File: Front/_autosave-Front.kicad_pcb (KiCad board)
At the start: 2 copper layers, 40 x 40 mm, 42 parts, among them J1 USB_B_Micro, Q1 BC849, Q2 BC849, SW1 SW_DPDT_x2, U1 CH340C, U10 ESP32-WROOM-32, U2 CJVL53L0XV2, U3 SPX3819M5-L-3-3

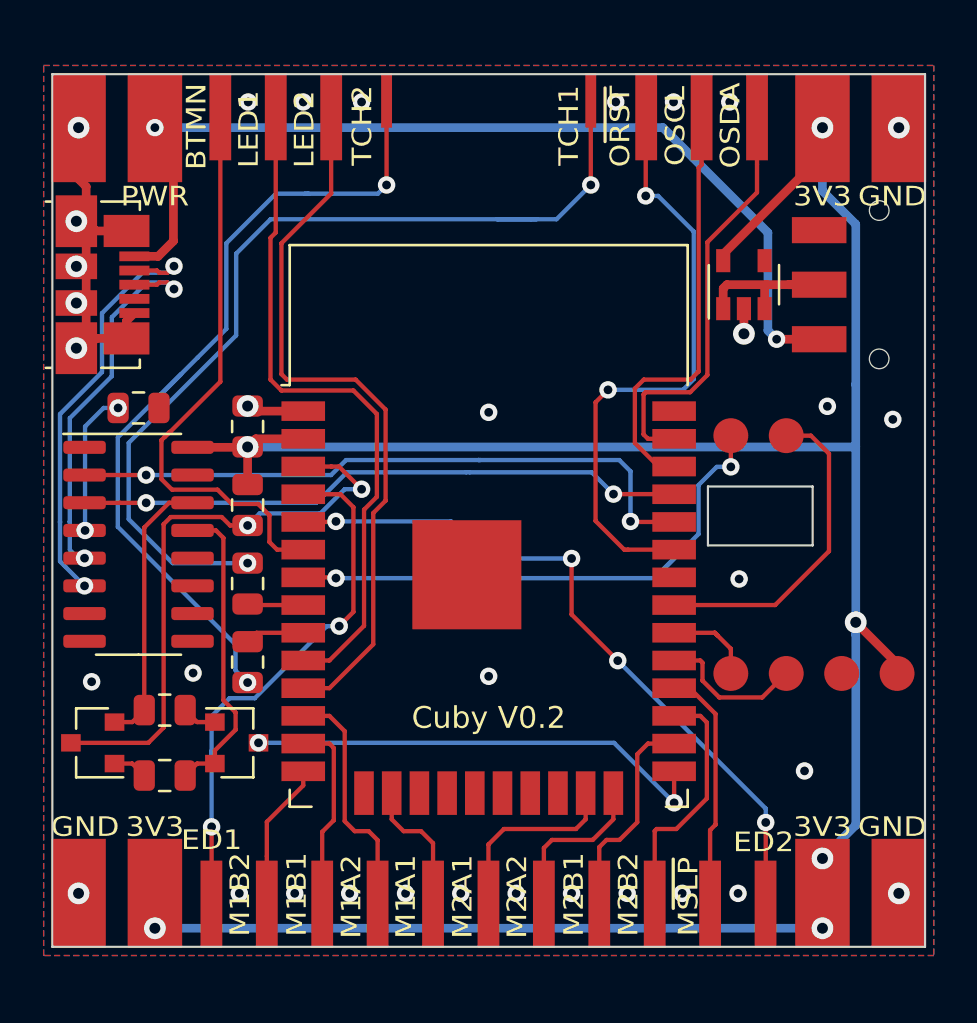
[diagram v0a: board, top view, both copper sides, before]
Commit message: updated bottom (motor placement, sharp sensor), front redesign, start op top redesign
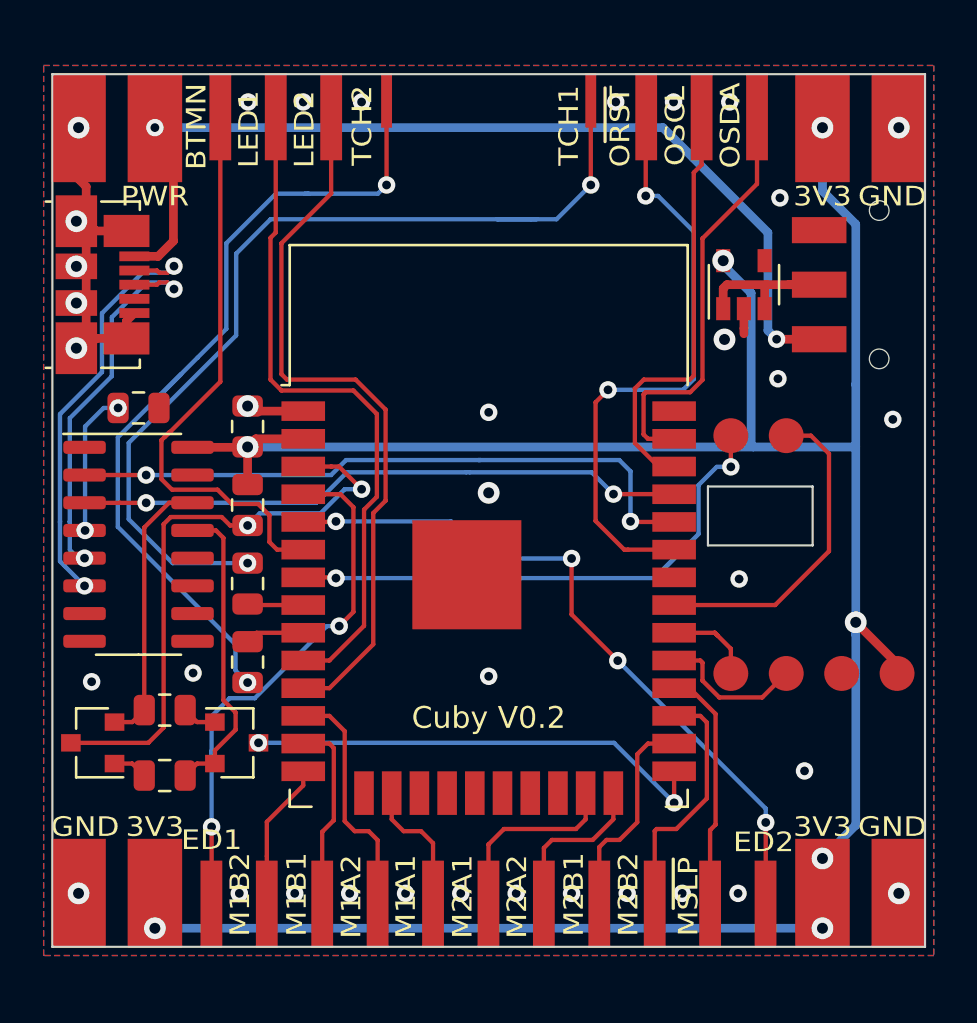
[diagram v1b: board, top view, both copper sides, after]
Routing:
- net +3V3: track 111.3 -> 113.7 mm, vias 6 -> 7
- net GND: vias 34 -> 36
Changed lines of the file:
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@@
     (thickness 1.6)
     (drawings 9)
-    (tracks 418)
+    (tracks 423)
     (zones 0)
     (modules 42)
@@
   (via (at 204.475 104.275) (size 0.8) (drill 0.4) (layers F.Cu B.Cu) (net 1))
   (via (at 221.325 104.275) (size 0.8) (drill 0.4) (layers F.Cu B.Cu) (net 1))
-  (via (at 227.2 114.9) (size 1) (drill 0.5) (layers F.Cu B.Cu) (net 1))
+  (via (at 226.31 115.16) (size 1) (drill 0.5) (layers F.Cu B.Cu) (net 1))
   (segment (start 227.2 113.75) (end 227.2 114.65) (width 0.4) (layer F.Cu) (net 1) (status 10))
   (segment (start 227.2 114.65) (end 227.2 114.9) (width 0.4) (layer F.Cu) (net 1))
@@
   (via (at 204.45 118.2125) (size 1) (drill 0.5) (layers F.Cu B.Cu) (net 1) (status 30))
   (via (at 234.025 118.825) (size 0.8) (drill 0.4) (layers F.Cu B.Cu) (net 1))
-  (via (at 231.025 118.225) (size 0.8) (drill 0.4) (layers F.Cu B.Cu) (net 1))
+  (via (at 228.76 116.96) (size 0.8) (drill 0.4) (layers F.Cu B.Cu) (net 1))
+  (via (at 228.85 108.67) (size 0.8) (drill 0.4) (layers F.Cu B.Cu) (net 1))
+  (via (at 215.5 122.19) (size 1) (drill 0.5) (layers F.Cu B.Cu) (net 1))
   (via (at 197.00001 123.915) (size 0.8) (drill 0.4) (layers F.Cu B.Cu) (net 2) (status 30))
   (via (at 198.5125 118.3) (size 0.8) (drill 0.4) (layers F.Cu B.Cu) (net 2) (status 30))
@@
   (segment (start 230.8 108.35) (end 232.325 109.875) (width 0.4) (layer B.Cu) (net 4))
   (segment (start 230.8 105.45) (end 230.8 108.35) (width 0.4) (layer B.Cu) (net 4))
-  (segment (start 226.25 111.25) (end 226.25 111.55) (width 0.4) (layer F.Cu) (net 4) (status 30))
-  (segment (start 230.8 106.7) (end 226.25 111.25) (width 0.4) (layer F.Cu) (net 4) (status 30))
   (segment (start 230.8 105.45) (end 230.8 106.7) (width 0.4) (layer F.Cu) (net 4) (status 30))
   (via (at 204.45 120.0875) (size 1) (drill 0.5) (layers F.Cu B.Cu) (net 4) (status 30))
@@
   (segment (start 232.325 120.075) (end 232.325 128.125) (width 0.4) (layer B.Cu) (net 4))
   (segment (start 232.3125 120.0875) (end 232.325 120.075) (width 0.4) (layer B.Cu) (net 4))
-  (segment (start 204.45 120.0875) (end 232.3125 120.0875) (width 0.4) (layer B.Cu) (net 4))
+  (via (at 226.25 111.55) (size 1) (drill 0.5) (layers F.Cu B.Cu) (net 4))
+  (segment (start 226.25 111.755) (end 227.53 113.035) (width 0.4) (layer B.Cu) (net 4))
+  (segment (start 226.25 111.55) (end 226.25 111.755) (width 0.4) (layer B.Cu) (net 4))
+  (segment (start 227.53 119.99) (end 227.6275 120.0875) (width 0.4) (layer B.Cu) (net 4))
+  (segment (start 227.53 113.035) (end 227.53 119.99) (width 0.4) (layer B.Cu) (net 4))
+  (segment (start 204.45 120.0875) (end 227.6275 120.0875) (width 0.4) (layer B.Cu) (net 4))
+  (segment (start 227.6275 120.0875) (end 232.3125 120.0875) (width 0.4) (layer B.Cu) (net 4))
   (segment (start 203.65 123.6875) (end 203.2625 123.3) (width 0.2) (layer F.Cu) (net 5))
   (segment (start 204.45 123.6875) (end 203.65 123.6875) (width 0.2) (layer F.Cu) (net 5) (status 10))
@@
   (via (at 221.417157 129.882843) (size 0.8) (drill 0.4) (layers F.Cu B.Cu) (net 17))
   (segment (start 221.417157 129.882843) (end 228.2 136.665685) (width 0.2) (layer B.Cu) (net 17))
-  (segment (start 222.8 119.715) (end 222.599999 119.514999) (width 0.2) (layer F.Cu) (net 18))
-  (segment (start 224 119.715) (end 222.8 119.715) (width 0.2) (layer F.Cu) (net 18))
-  (segment (start 222.599999 119.514999) (end 222.599999 117.674999) (width 0.2) (layer F.Cu) (net 18))
-  (segment (start 222.599999 117.674999) (end 222.694998 117.58) (width 0.2) (layer F.Cu) (net 18))
-  (segment (start 227.8 108.424998) (end 227.8 107.15) (width 0.2) (layer F.Cu) (net 18))
-  (segment (start 227.8 107.15) (end 227.8 104.95) (width 0.2) (layer F.Cu) (net 18))
-  (segment (start 225.524999 110.699999) (end 227.8 108.424998) (width 0.2) (layer F.Cu) (net 18))
-  (segment (start 225.524999 116.790701) (end 225.524999 110.699999) (width 0.2) (layer F.Cu) (net 18))
-  (segment (start 224.7357 117.58) (end 225.524999 116.790701) (width 0.2) (layer F.Cu) (net 18))
-  (segment (start 222.694998 117.58) (end 224.7357 117.58) (width 0.2) (layer F.Cu) (net 18))
+  (segment (start 222.599999 119.514999) (end 222.8 119.715) (width 0.2) (layer F.Cu) (net 18))
+  (segment (start 222.599999 117.674999) (end 222.599999 119.514999) (width 0.2) (layer F.Cu) (net 18))
+  (segment (start 227.8 108.03) (end 225.30002 110.52998) (width 0.2) (layer F.Cu) (net 18))
+  (segment (start 227.8 104.95) (end 227.8 108.03) (width 0.2) (layer F.Cu) (net 18))
+  (segment (start 225.30002 110.52998) (end 225.30002 117.01568) (width 0.2) (layer F.Cu) (net 18))
+  (segment (start 225.30002 117.01568) (end 224.7357 117.58) (width 0.2) (layer F.Cu) (net 18))
+  (segment (start 222.8 119.715) (end 224 119.715) (width 0.2) (layer F.Cu) (net 18))
+  (segment (start 224.7357 117.58) (end 222.694998 117.58) (width 0.2) (layer F.Cu) (net 18))
+  (segment (start 222.694998 117.58) (end 222.599999 117.674999) (width 0.2) (layer F.Cu) (net 18))
+  (segment (start 225.26 107.15) (end 225.26 104.95) (width 0.2) (layer F.Cu) (net 19))
+  (segment (start 224.90001 107.50999) (end 225.26 107.15) (width 0.2) (layer F.Cu) (net 19))
+  (segment (start 224.90001 116.82427) (end 224.90001 107.50999) (width 0.2) (layer F.Cu) (net 19))
+  (segment (start 223.279998 120.985) (end 222.199988 119.90499) (width 0.2) (layer F.Cu) (net 19))
+  (segment (start 224 120.985) (end 223.279998 120.985) (width 0.2) (layer F.Cu) (net 19))
   (segment (start 222.199988 119.90499) (end 222.199988 117.410012) (width 0.2) (layer F.Cu) (net 19))
-  (segment (start 224 120.985) (end 223.279998 120.985) (width 0.2) (layer F.Cu) (net 19))
-  (segment (start 223.279998 120.985) (end 222.199988 119.90499) (width 0.2) (layer F.Cu) (net 19))
-  (segment (start 222.60999 117.00001) (end 224.74999 117.00001) (width 0.2) (layer F.Cu) (net 19))
+  (segment (start 222.60999 117.00001) (end 224.72427 117.00001) (width 0.2) (layer F.Cu) (net 19))
   (segment (start 222.199988 117.410012) (end 222.60999 117.00001) (width 0.2) (layer F.Cu) (net 19))
-  (segment (start 225.26 107.15) (end 225.26 104.95) (width 0.2) (layer F.Cu) (net 19))
-  (segment (start 225.124988 116.625012) (end 225.124988 107.285012) (width 0.2) (layer F.Cu) (net 19))
-  (segment (start 224.74999 117.00001) (end 225.124988 116.625012) (width 0.2) (layer F.Cu) (net 19))
-  (segment (start 225.124988 107.285012) (end 225.26 107.15) (width 0.2) (layer F.Cu) (net 19))
+  (segment (start 224.72427 117.00001) (end 224.90001 116.82427) (width 0.2) (layer F.Cu) (net 19))
   (segment (start 224 124.795) (end 221.88 124.795) (width 0.2) (layer F.Cu) (net 20))
   (segment (start 221.88 124.795) (end 221.715 124.795) (width 0.2) (layer F.Cu) (net 20))
